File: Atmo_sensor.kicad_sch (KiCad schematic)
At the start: 1 part, among them J5 Conn_01x05

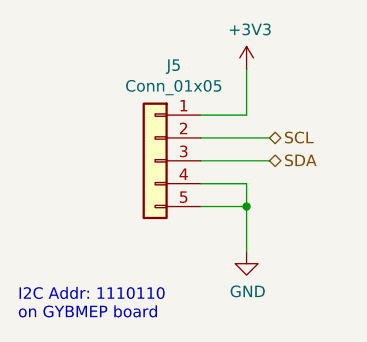
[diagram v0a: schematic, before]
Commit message: Move to KiCad v6, redesign circuit for chamber
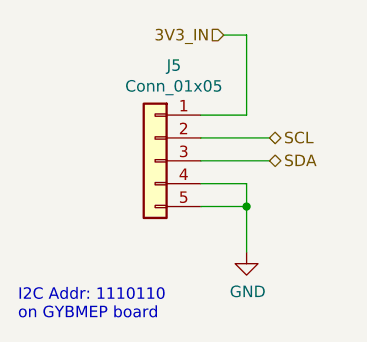
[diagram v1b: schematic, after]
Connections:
- net +3V3 renamed 3V3_IN
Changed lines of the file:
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@@
     (stroke (width 0) (type default) (color 0 0 0 0))
   )
-  (wire (pts (xy 152.4 93.98) (xy 152.4 88.9))
+  (wire (pts (xy 152.4 85.09) (xy 152.4 93.98))
     (stroke (width 0) (type default) (color 0 0 0 0))
   )
@@
     (stroke (width 0) (type default) (color 0 0 0 0))
   )
+  (wire (pts (xy 149.86 85.09) (xy 152.4 85.09))
+    (stroke (width 0) (type default) (color 0 0 0 0))
+  )
   (wire (pts (xy 152.4 101.6) (xy 152.4 104.14))
     (stroke (width 0) (type default) (color 0 0 0 0))
@@
     (effects (font (size 1.27 1.27)) (justify left))
   )
+  (hierarchical_label "3V3_IN" (shape input) (at 149.86 85.09 180)
+    (effects (font (size 1.27 1.27)) (justify right))
+  )
   (hierarchical_label "SCL" (shape bidirectional) (at 154.94 96.52 0)
     (effects (font (size 1.27 1.27)) (justify left))
   )
-  (symbol (lib_id "power:+3V3") (at 152.4 88.9 0) (unit 1)
-    (in_bom yes) (on_board yes)
-    (property "Reference" "#PWR011" (id 0) (at 152.4 92.71 0)
-      (effects (font (size 1.27 1.27)) hide)
-    )
-    (property "Value" "+3V3" (id 1) (at 152.781 84.5058 0))
-    (property "Footprint" "" (id 2) (at 152.4 88.9 0)
-      (effects (font (size 1.27 1.27)) hide)
-    )
-    (property "Datasheet" "" (id 3) (at 152.4 88.9 0)
-      (effects (font (size 1.27 1.27)) hide)
-    )
-    (pin "1")
-  )
   (symbol (lib_id "power:GND") (at 152.4 109.22 0) (unit 1)

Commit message: Finalize schematic
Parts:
- renumbered J5 to J10
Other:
- title: (none) -> CO2 Chamber - Atmospheric Sensor Connector
- moved on the sheet: J10
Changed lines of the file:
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@@
 (kicad_sch (version 20211123) (generator eeschema)
   (paper "A4")
-  (junction (at 152.4 104.14) (diameter 0) (color 0 0 0 0)
+  (title_block
+    (title "CO2 Chamber - Atmospheric Sensor Connector")
+    (date "2022-05-20")
+    (rev "1")
   )
-  (wire (pts (xy 147.32 99.06) (xy 154.94 99.06))
+  (junction (at 154.94 104.14) (diameter 0) (color 0 0 0 0)
+  )
+  (wire (pts (xy 149.86 99.06) (xy 157.48 99.06))
     (stroke (width 0) (type default) (color 0 0 0 0))
   )
-  (wire (pts (xy 152.4 85.09) (xy 152.4 93.98))
+  (wire (pts (xy 154.94 85.09) (xy 154.94 93.98))
     (stroke (width 0) (type default) (color 0 0 0 0))
   )
-  (wire (pts (xy 152.4 101.6) (xy 147.32 101.6))
+  (wire (pts (xy 154.94 101.6) (xy 149.86 101.6))
     (stroke (width 0) (type default) (color 0 0 0 0))
   )
-  (wire (pts (xy 147.32 93.98) (xy 152.4 93.98))
+  (wire (pts (xy 149.86 93.98) (xy 154.94 93.98))
     (stroke (width 0) (type default) (color 0 0 0 0))
   )
-  (wire (pts (xy 147.32 96.52) (xy 154.94 96.52))
+  (wire (pts (xy 149.86 96.52) (xy 157.48 96.52))
     (stroke (width 0) (type default) (color 0 0 0 0))
   )
-  (wire (pts (xy 152.4 104.14) (xy 152.4 109.22))
+  (wire (pts (xy 154.94 104.14) (xy 154.94 109.22))
     (stroke (width 0) (type default) (color 0 0 0 0))
   )
-  (wire (pts (xy 147.32 104.14) (xy 152.4 104.14))
+  (wire (pts (xy 149.86 104.14) (xy 154.94 104.14))
     (stroke (width 0) (type default) (color 0 0 0 0))
   )
-  (wire (pts (xy 149.86 85.09) (xy 152.4 85.09))
+  (wire (pts (xy 152.4 85.09) (xy 154.94 85.09))
     (stroke (width 0) (type default) (color 0 0 0 0))
   )
-  (wire (pts (xy 152.4 101.6) (xy 152.4 104.14))
+  (wire (pts (xy 154.94 101.6) (xy 154.94 104.14))
     (stroke (width 0) (type default) (color 0 0 0 0))
   )
-  (text "I2C Addr: 1110110\non GYBMEP board" (at 127 116.84 0)
+  (text "I2C Addr: 1110110\non GYBMEP board" (at 129.54 116.84 0)
     (effects (font (size 1.27 1.27)) (justify left bottom))
   )
-  (hierarchical_label "SDA" (shape bidirectional) (at 154.94 99.06 0)
+  (hierarchical_label "SDA" (shape bidirectional) (at 157.48 99.06 0)
     (effects (font (size 1.27 1.27)) (justify left))
   )
-  (hierarchical_label "3V3_IN" (shape input) (at 149.86 85.09 180)
+  (hierarchical_label "3V3_IN" (shape input) (at 152.4 85.09 180)
     (effects (font (size 1.27 1.27)) (justify right))
   )
-  (hierarchical_label "SCL" (shape bidirectional) (at 154.94 96.52 0)
+  (hierarchical_label "SCL" (shape bidirectional) (at 157.48 96.52 0)
     (effects (font (size 1.27 1.27)) (justify left))
   )
-  (symbol (lib_id "power:GND") (at 152.4 109.22 0) (unit 1)
+  (symbol (lib_id "power:GND") (at 154.94 109.22 0) (unit 1)
     (in_bom yes) (on_board yes)
-    (property "Reference" "#PWR012" (id 0) (at 152.4 115.57 0)
+    (property "Reference" "#PWR028" (id 0) (at 154.94 115.57 0)
       (effects (font (size 1.27 1.27)) hide)
     )
-    (property "Value" "GND" (id 1) (at 152.527 113.6142 0))
-    (property "Footprint" "" (id 2) (at 152.4 109.22 0)
+    (property "Value" "GND" (id 1) (at 155.067 113.6142 0))
+    (property "Footprint" "" (id 2) (at 154.94 109.22 0)
       (effects (font (size 1.27 1.27)) hide)
     )
-    (property "Datasheet" "" (id 3) (at 152.4 109.22 0)
+    (property "Datasheet" "" (id 3) (at 154.94 109.22 0)
       (effects (font (size 1.27 1.27)) hide)
     )
     (pin "1")
   )
-  (symbol (lib_id "Connector_Generic:Conn_01x05") (at 142.24 99.06 0) (mirror y) (unit 1)
+  (symbol (lib_id "Connector_Generic:Conn_01x05") (at 144.78 99.06 0) (mirror y) (unit 1)
     (in_bom yes) (on_board yes)
-    (property "Reference" "J5" (id 0) (at 144.3228 88.4682 0))
-    (property "Value" "Conn_01x05" (id 1) (at 144.3228 90.7796 0))
-    (property "Footprint" "Connector_JST:JST_XH_B5B-XH-AM_1x05_P2.50mm_Vertical" (id 2) (at 142.24 99.06 0)
+    (property "Reference" "J10" (id 0) (at 146.8628 88.4682 0))
+    (property "Value" "Conn_01x05" (id 1) (at 146.8628 90.7796 0))
+    (property "Footprint" "Connector_JST:JST_XH_B5B-XH-AM_1x05_P2.50mm_Vertical" (id 2) (at 144.78 99.06 0)
       (effects (font (size 1.27 1.27)) hide)
     )
-    (property "Datasheet" "~" (id 3) (at 142.24 99.06 0)
+    (property "Datasheet" "~" (id 3) (at 144.78 99.06 0)
       (effects (font (size 1.27 1.27)) hide)
     )

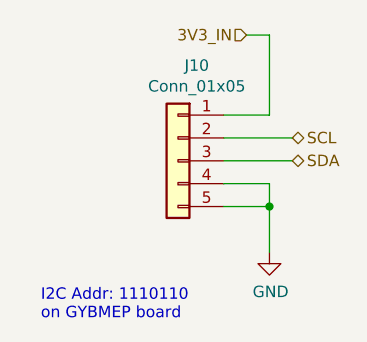
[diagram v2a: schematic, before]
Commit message: Finish PCB layout
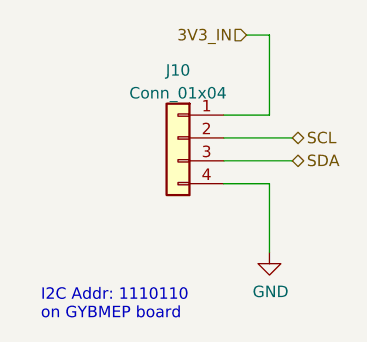
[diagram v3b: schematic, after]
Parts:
- removed J10: Conn_01x05, Connector_JST:JST_XH_B5B-XH-AM_1x05_P2.50mm_Vertical, symbol Connector_Generic:Conn_01x05
- added J10: Conn_01x04, Connector_JST:JST_XH_B4B-XH-A_1x04_P2.50mm_Vertical, symbol Connector_Generic:Conn_01x04
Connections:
- net 3V3_IN: now also J10.1 (Pin_1)
- net GND: now also J10.4 (Pin_4)
- net SCL: now also J10.2 (Pin_2)
- net SDA: now also J10.3 (Pin_3)
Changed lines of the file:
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@@
     (rev "1")
-  )
-  (junction (at 154.94 104.14) (diameter 0) (color 0 0 0 0)
   )
   (wire (pts (xy 149.86 99.06) (xy 157.48 99.06))
@@
     (stroke (width 0) (type default) (color 0 0 0 0))
   )
-  (wire (pts (xy 154.94 104.14) (xy 154.94 109.22))
-    (stroke (width 0) (type default) (color 0 0 0 0))
-  )
-  (wire (pts (xy 149.86 104.14) (xy 154.94 104.14))
+  (wire (pts (xy 154.94 101.6) (xy 154.94 109.22))
     (stroke (width 0) (type default) (color 0 0 0 0))
   )
   (wire (pts (xy 152.4 85.09) (xy 154.94 85.09))
-    (stroke (width 0) (type default) (color 0 0 0 0))
-  )
-  (wire (pts (xy 154.94 101.6) (xy 154.94 104.14))
     (stroke (width 0) (type default) (color 0 0 0 0))
   )
@@
     (pin "1")
   )
-  (symbol (lib_id "Connector_Generic:Conn_01x05") (at 144.78 99.06 0) (mirror y) (unit 1)
-    (in_bom yes) (on_board yes)
-    (property "Reference" "J10" (id 0) (at 146.8628 88.4682 0))
-    (property "Value" "Conn_01x05" (id 1) (at 146.8628 90.7796 0))
-    (property "Footprint" "Connector_JST:JST_XH_B5B-XH-AM_1x05_P2.50mm_Vertical" (id 2) (at 144.78 99.06 0)
+  (symbol (lib_id "Connector_Generic:Conn_01x04") (at 144.78 96.52 0) (mirror y) (unit 1)
+    (in_bom yes) (on_board yes) (fields_autoplaced)
+    (property "Reference" "J10" (id 0) (at 144.78 89.0102 0))
+    (property "Value" "Conn_01x04" (id 1) (at 144.78 91.5471 0))
+    (property "Footprint" "Connector_JST:JST_XH_B4B-XH-A_1x04_P2.50mm_Vertical" (id 2) (at 144.78 96.52 0)
       (effects (font (size 1.27 1.27)) hide)
     )
-    (property "Datasheet" "~" (id 3) (at 144.78 99.06 0)
+    (property "Datasheet" "~" (id 3) (at 144.78 96.52 0)
+      (effects (font (size 1.27 1.27)) hide)
+    )
+    (property "LCSC" "C37815" (id 4) (at 144.78 96.52 0)
       (effects (font (size 1.27 1.27)) hide)
     )
@@
     (pin "3")
     (pin "4")
-    (pin "5")
   )
 )

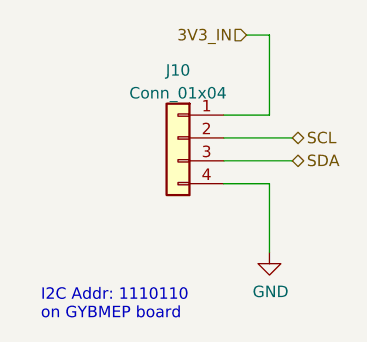
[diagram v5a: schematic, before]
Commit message: Add 5V boost converter and begin redesign of PCB
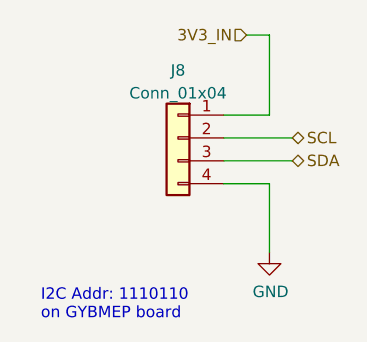
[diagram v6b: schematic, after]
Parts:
- renumbered J10 to J8
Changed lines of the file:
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@@
   (symbol (lib_id "power:GND") (at 154.94 109.22 0) (unit 1)
     (in_bom yes) (on_board yes)
-    (property "Reference" "#PWR034" (id 0) (at 154.94 115.57 0)
+    (property "Reference" "#PWR046" (id 0) (at 154.94 115.57 0)
       (effects (font (size 1.27 1.27)) hide)
     )
@@
   (symbol (lib_id "Connector_Generic:Conn_01x04") (at 144.78 96.52 0) (mirror y) (unit 1)
     (in_bom yes) (on_board yes) (fields_autoplaced)
-    (property "Reference" "J10" (id 0) (at 144.78 89.0102 0))
+    (property "Reference" "J8" (id 0) (at 144.78 89.0102 0))
     (property "Value" "Conn_01x04" (id 1) (at 144.78 91.5471 0))
     (property "Footprint" "Connector_JST:JST_XH_B4B-XH-A_1x04_P2.50mm_Vertical" (id 2) (at 144.78 96.52 0)

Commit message: Finish component placement
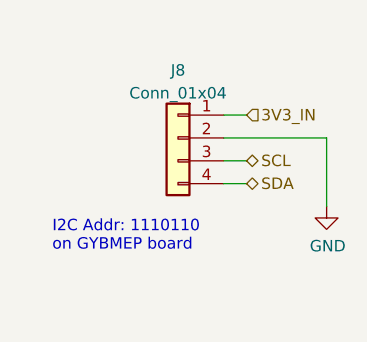
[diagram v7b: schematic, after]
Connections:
- net GND: now also J8.2 (Pin_2); no longer J8.4 (Pin_4)
- net SCL: now also J8.3 (Pin_3); no longer J8.2 (Pin_2)
- net SDA: now also J8.4 (Pin_4); no longer J8.3 (Pin_3)
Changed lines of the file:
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@@
     (rev "2")
   )
-  (wire (pts (xy 149.86 99.06) (xy 157.48 99.06))
+  (wire (pts (xy 149.86 93.98) (xy 152.4 93.98))
     (stroke (width 0) (type default) (color 0 0 0 0))
   )
-  (wire (pts (xy 154.94 85.09) (xy 154.94 93.98))
+  (wire (pts (xy 149.86 99.06) (xy 152.4 99.06))
     (stroke (width 0) (type default) (color 0 0 0 0))
   )
-  (wire (pts (xy 154.94 101.6) (xy 149.86 101.6))
+  (wire (pts (xy 161.29 96.52) (xy 149.86 96.52))
     (stroke (width 0) (type default) (color 0 0 0 0))
   )
-  (wire (pts (xy 149.86 93.98) (xy 154.94 93.98))
+  (wire (pts (xy 149.86 101.6) (xy 152.4 101.6))
     (stroke (width 0) (type default) (color 0 0 0 0))
   )
-  (wire (pts (xy 149.86 96.52) (xy 157.48 96.52))
+  (wire (pts (xy 161.29 96.52) (xy 161.29 104.14))
     (stroke (width 0) (type default) (color 0 0 0 0))
   )
-  (wire (pts (xy 154.94 101.6) (xy 154.94 109.22))
-    (stroke (width 0) (type default) (color 0 0 0 0))
-  )
-  (wire (pts (xy 152.4 85.09) (xy 154.94 85.09))
-    (stroke (width 0) (type default) (color 0 0 0 0))
-  )
-  (text "I2C Addr: 1110110\non GYBMEP board" (at 129.54 116.84 0)
+  (text "I2C Addr: 1110110\non GYBMEP board" (at 130.81 109.22 0)
     (effects (font (size 1.27 1.27)) (justify left bottom))
   )
-  (hierarchical_label "SDA" (shape bidirectional) (at 157.48 99.06 0)
+  (hierarchical_label "SDA" (shape bidirectional) (at 152.4 101.6 0)
     (effects (font (size 1.27 1.27)) (justify left))
   )
-  (hierarchical_label "3V3_IN" (shape input) (at 152.4 85.09 180)
-    (effects (font (size 1.27 1.27)) (justify right))
-  )
-  (hierarchical_label "SCL" (shape bidirectional) (at 157.48 96.52 0)
+  (hierarchical_label "3V3_IN" (shape input) (at 152.4 93.98 0)
     (effects (font (size 1.27 1.27)) (justify left))
   )
-  (symbol (lib_id "power:GND") (at 154.94 109.22 0) (unit 1)
+  (hierarchical_label "SCL" (shape bidirectional) (at 152.4 99.06 0)
+    (effects (font (size 1.27 1.27)) (justify left))
+  )
+  (symbol (lib_id "power:GND") (at 161.29 104.14 0) (unit 1)
     (in_bom yes) (on_board yes)
-    (property "Reference" "#PWR046" (id 0) (at 154.94 115.57 0)
+    (property "Reference" "#PWR046" (id 0) (at 161.29 110.49 0)
       (effects (font (size 1.27 1.27)) hide)
     )
-    (property "Value" "GND" (id 1) (at 155.067 113.6142 0))
-    (property "Footprint" "" (id 2) (at 154.94 109.22 0)
+    (property "Value" "GND" (id 1) (at 161.417 108.5342 0))
+    (property "Footprint" "" (id 2) (at 161.29 104.14 0)
       (effects (font (size 1.27 1.27)) hide)
     )
-    (property "Datasheet" "" (id 3) (at 154.94 109.22 0)
+    (property "Datasheet" "" (id 3) (at 161.29 104.14 0)
       (effects (font (size 1.27 1.27)) hide)
     )
